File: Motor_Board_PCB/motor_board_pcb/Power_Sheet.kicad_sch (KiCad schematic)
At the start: 16 parts, among them J4 Barrel_Jack, U3 AP2112K-3.3TRG1, U4 AP63205WU-7

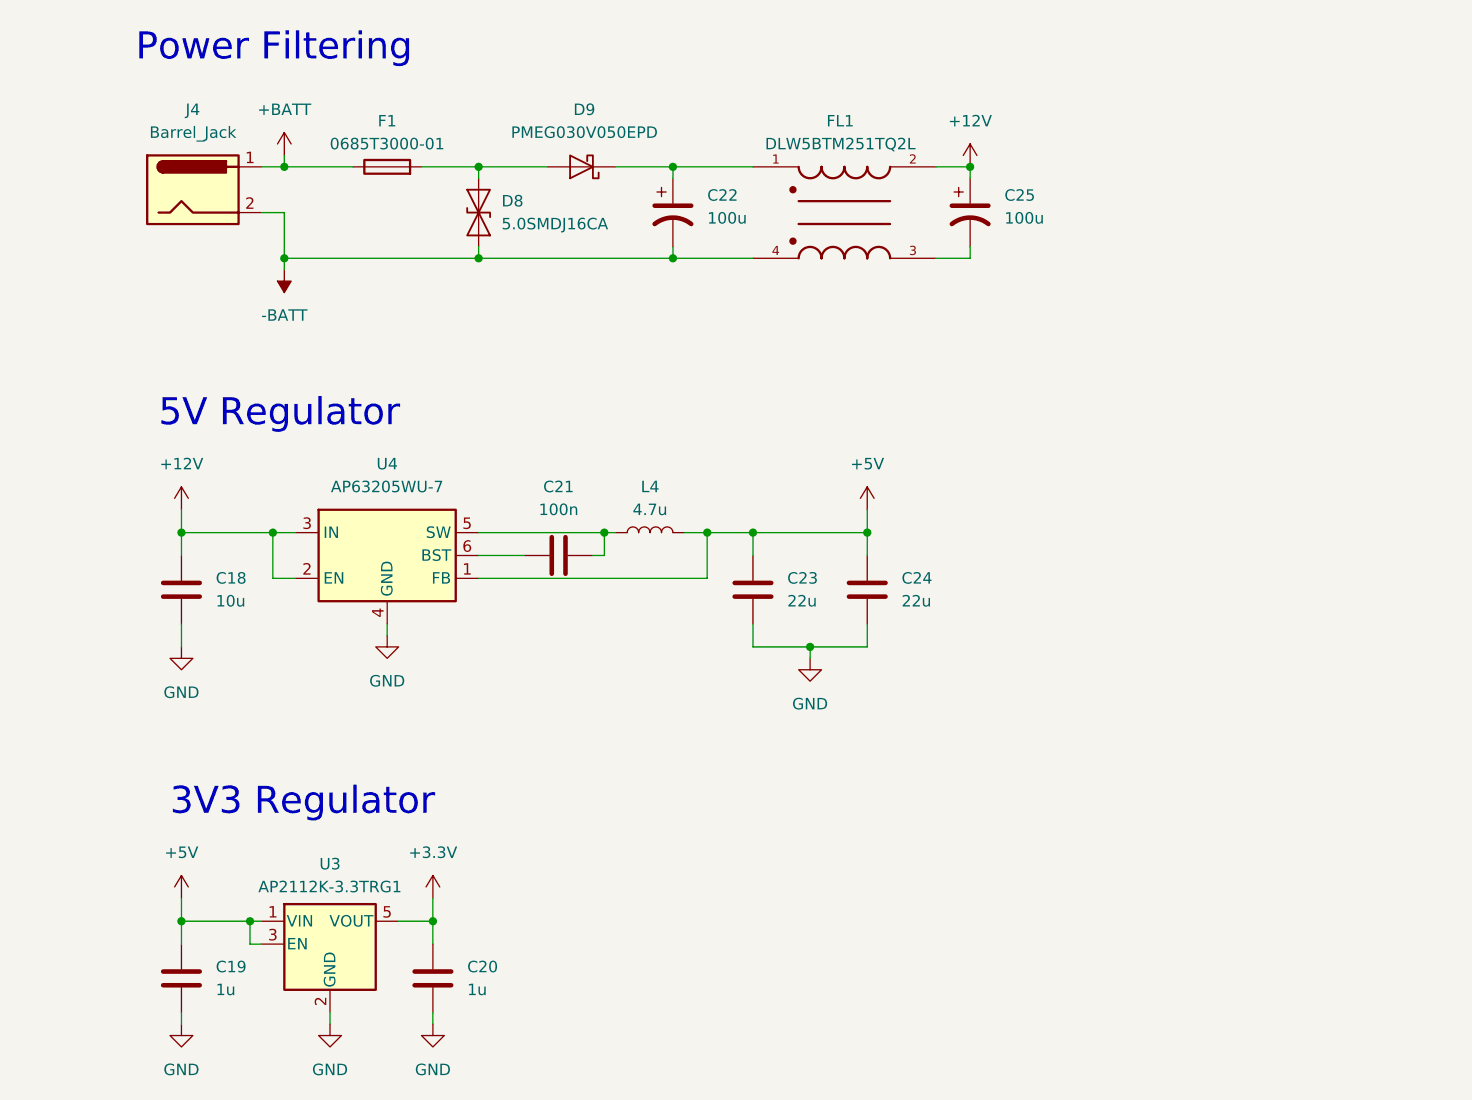
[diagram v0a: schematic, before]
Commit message: Added footprints for almost all components
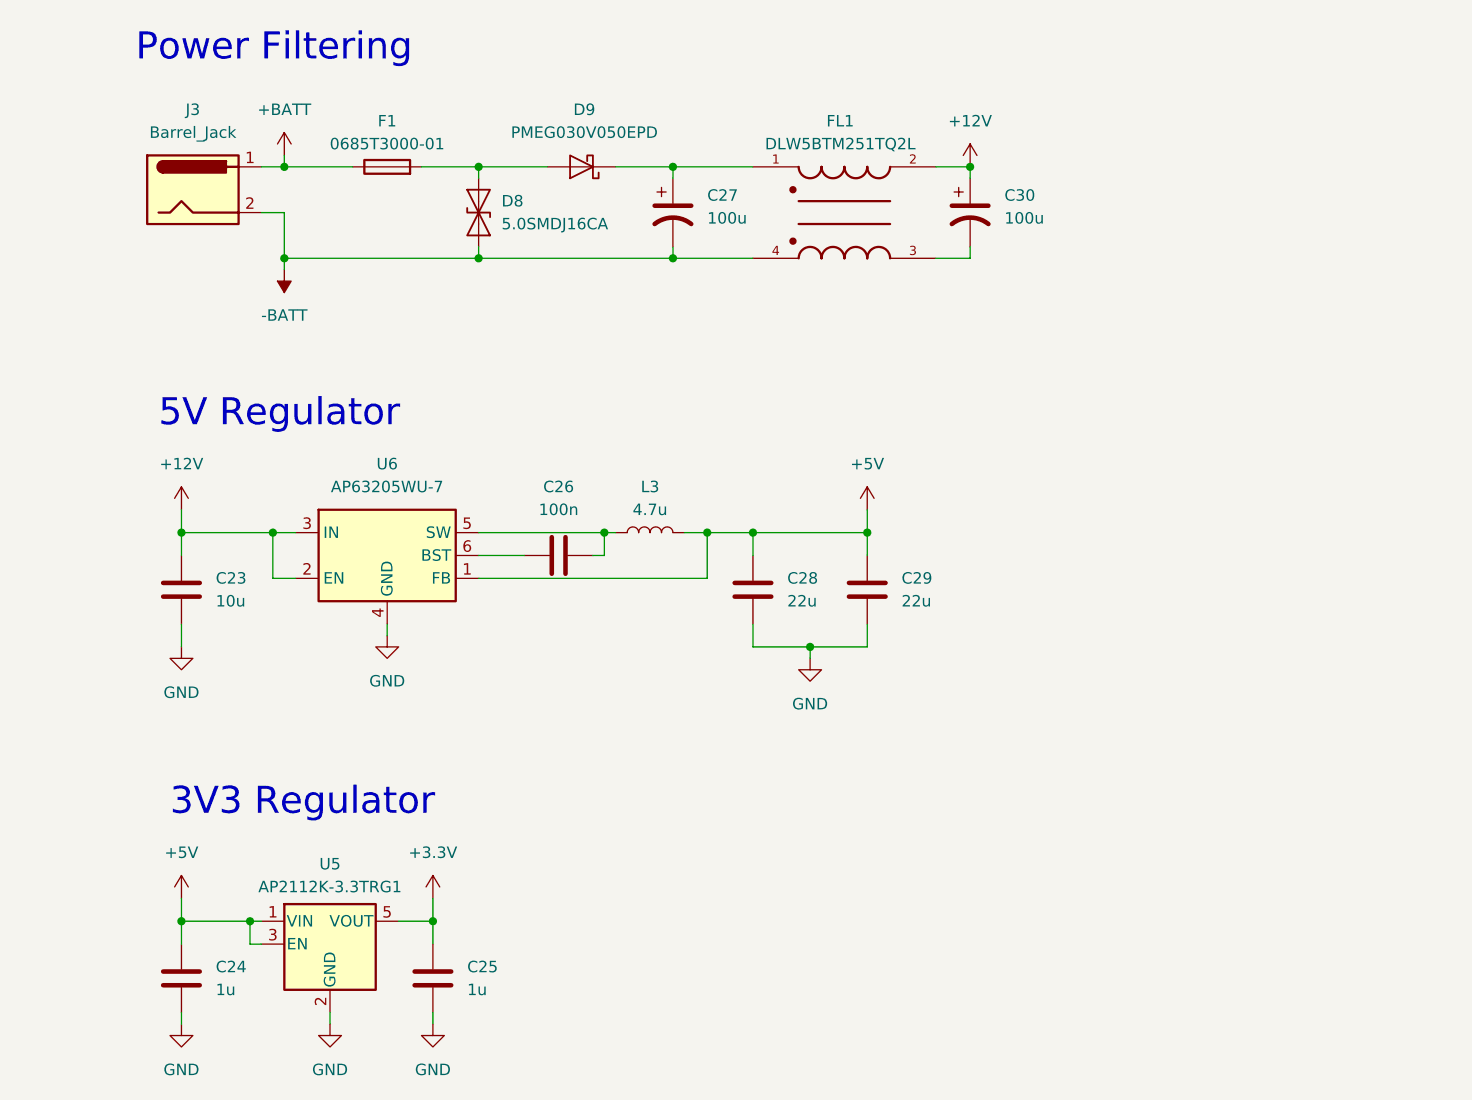
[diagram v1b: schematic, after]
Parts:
- removed J4: Barrel_Jack, symbol Connector:Barrel_Jack
- added J3: Barrel_Jack, Connector_BarrelJack:BarrelJack_CUI_PJ-063AH_Horizontal, symbol Connector:Barrel_Jack
- C23: renamed from C18; footprint (none) -> Capacitor_SMD:C_0603_1608Metric
- C24: renamed from C19; footprint (none) -> Capacitor_SMD:C_0603_1608Metric
- C25: renamed from C20; footprint (none) -> Capacitor_SMD:C_0603_1608Metric
- C26: renamed from C21; footprint (none) -> Capacitor_SMD:C_0603_1608Metric
- C27: renamed from C22; footprint (none) -> Capacitor_SMD:C_0603_1608Metric
- C28: renamed from C23; footprint (none) -> Capacitor_SMD:C_0603_1608Metric
- C29: renamed from C24; footprint (none) -> Capacitor_SMD:C_0603_1608Metric
- C30: renamed from C25; footprint (none) -> Capacitor_SMD:C_0603_1608Metric
- D8: footprint (none) -> Diode_SMD:D_0603_1608Metric
- F1: footprint (none) -> Fuse:Fuse_0603_1608Metric
- FL1: footprint DLW5BTM251TQ2L:FIL_DLW5BTM251TQ2L -> (none)
- renumbered L4 to L3, U3 to U5, U4 to U6
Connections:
- net +BATT: now also J3.1
- net -BATT: now also J3.2

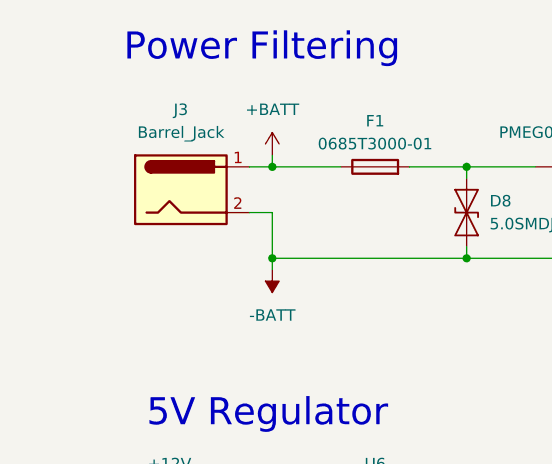
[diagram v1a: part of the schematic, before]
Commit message: Added all other footprints... populated all components with NO errors or warnings :)
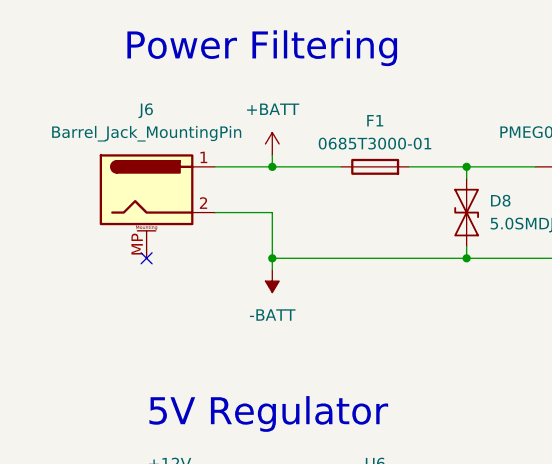
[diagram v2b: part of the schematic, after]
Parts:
- removed J3: Barrel_Jack, Connector_BarrelJack:BarrelJack_CUI_PJ-063AH_Horizontal, symbol Connector:Barrel_Jack
- added J6: Barrel_Jack_MountingPin, Connector_BarrelJack:BarrelJack_CUI_PJ-063AH_Horizontal, symbol Connector:Barrel_Jack_MountingPin
- FL1: footprint (none) -> ~ALL:FIL_DLW5BTZ251TQ2L
- L3: footprint (none) -> ~ALL:INDC2520X120N
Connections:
- net +BATT: now also J6.1
- net -BATT: now also J6.2
- no-connect marks 0 -> 1
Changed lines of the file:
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@@
   (junction (at 68.58 132.08) (diameter 0) (color 0 0 0 0)
   )
+  (no_connect (at 38.1 58.42))
   (wire (pts (xy 104.14 101.6) (xy 110.49 101.6))
     (stroke (width 0) (type default))
@@
     (stroke (width 0) (type default))
   )
-  (wire (pts (xy 49.53 48.26) (xy 52.07 48.26))
+  (wire (pts (xy 45.72 48.26) (xy 52.07 48.26))
     (stroke (width 0) (type default))
   )
@@
     (stroke (width 0) (type default))
   )
-  (wire (pts (xy 49.53 53.34) (xy 52.07 53.34))
-    (stroke (width 0) (type default))
-  )
   (wire (pts (xy 73.66 49.53) (xy 73.66 48.26))
     (stroke (width 0) (type default))
@@
   )
   (wire (pts (xy 52.07 53.34) (xy 52.07 58.42))
+    (stroke (width 0) (type default))
+  )
+  (wire (pts (xy 45.72 53.34) (xy 52.07 53.34))
     (stroke (width 0) (type default))
   )
@@
     )
   )
+  (symbol (lib_id "Connector:Barrel_Jack_MountingPin") (at 38.1 50.8 0) (unit 1)
+    (in_bom yes) (on_board yes) (dnp no) (fields_autoplaced)
+    (property "Reference" "J6" (at 38.1 41.91 0)
+      (effects (font (size 1.27 1.27)))
+    )
+    (property "Value" "Barrel_Jack_MountingPin" (at 38.1 44.45 0)
+      (effects (font (size 1.27 1.27)))
+    )
+    (property "Footprint" "Connector_BarrelJack:BarrelJack_CUI_PJ-063AH_Horizontal" (at 39.37 51.816 0)
+      (effects (font (size 1.27 1.27)) hide)
+    )
+    (property "Datasheet" "~" (at 39.37 51.816 0)
+      (effects (font (size 1.27 1.27)) hide)
+    )
+    (pin "1")
+    (pin "2")
+    (pin "MP")
+    (instances
+      (project "motor_board_pcb"
+        (path "/4ad82a24-c992-45c9-b523-12e12bcd6ced/8b03500d-82ba-403b-affc-552426d5b4ea"
+          (reference "J6") (unit 1)
+        )
+      )
+    )
+  )
   (symbol (lib_id "DLW5BTM251TQ2L:DLW5BTM251TQ2L") (at 114.3 53.34 0) (unit 1)
     (in_bom yes) (on_board yes) (dnp no) (fields_autoplaced)
@@
       (effects (font (size 1.27 1.27)))
     )
-    (property "Footprint" "" (at 114.3 53.34 0)
+    (property "Footprint" "~ALL:FIL_DLW5BTZ251TQ2L" (at 114.3 53.34 0)
       (effects (font (size 1.27 1.27)) (justify bottom) hide)
     )
@@
         (path "/a439ee58-92e3-49e0-a19d-7c5a25d23ba1"
           (reference "#PWR?") (unit 1)
-        )
-      )
-    )
-  )
-  (symbol (lib_id "Connector:Barrel_Jack") (at 41.91 50.8 0) (unit 1)
-    (in_bom yes) (on_board yes) (dnp no) (fields_autoplaced)
-    (property "Reference" "J3" (at 41.91 41.91 0)
-      (effects (font (size 1.27 1.27)))
-    )
-    (property "Value" "Barrel_Jack" (at 41.91 44.45 0)
-      (effects (font (size 1.27 1.27)))
-    )
-    (property "Footprint" "Connector_BarrelJack:BarrelJack_CUI_PJ-063AH_Horizontal" (at 43.18 51.816 0)
-      (effects (font (size 1.27 1.27)) hide)
-    )
-    (property "Datasheet" "~" (at 43.18 51.816 0)
-      (effects (font (size 1.27 1.27)) hide)
-    )
-    (pin "1")
-    (pin "2")
-    (instances
-      (project "motor_board_pcb"
-        (path "/4ad82a24-c992-45c9-b523-12e12bcd6ced/8b03500d-82ba-403b-affc-552426d5b4ea"
-          (reference "J3") (unit 1)
-        )
-      )
-      (project "LocalDesign"
-        (path "/a439ee58-92e3-49e0-a19d-7c5a25d23ba1"
-          (reference "J?") (unit 1)
         )
       )
@@
       (effects (font (size 1.27 1.27)))
     )
-    (property "Footprint" "" (at 92.71 88.9 0)
-      (effects (font (size 1.27 1.27)) hide)
-    )
+    (property "Footprint" "~ALL:INDC2520X120N" (at 92.71 88.9 0)
+      (effects (font (size 1.27 1.27)) hide)
+    )

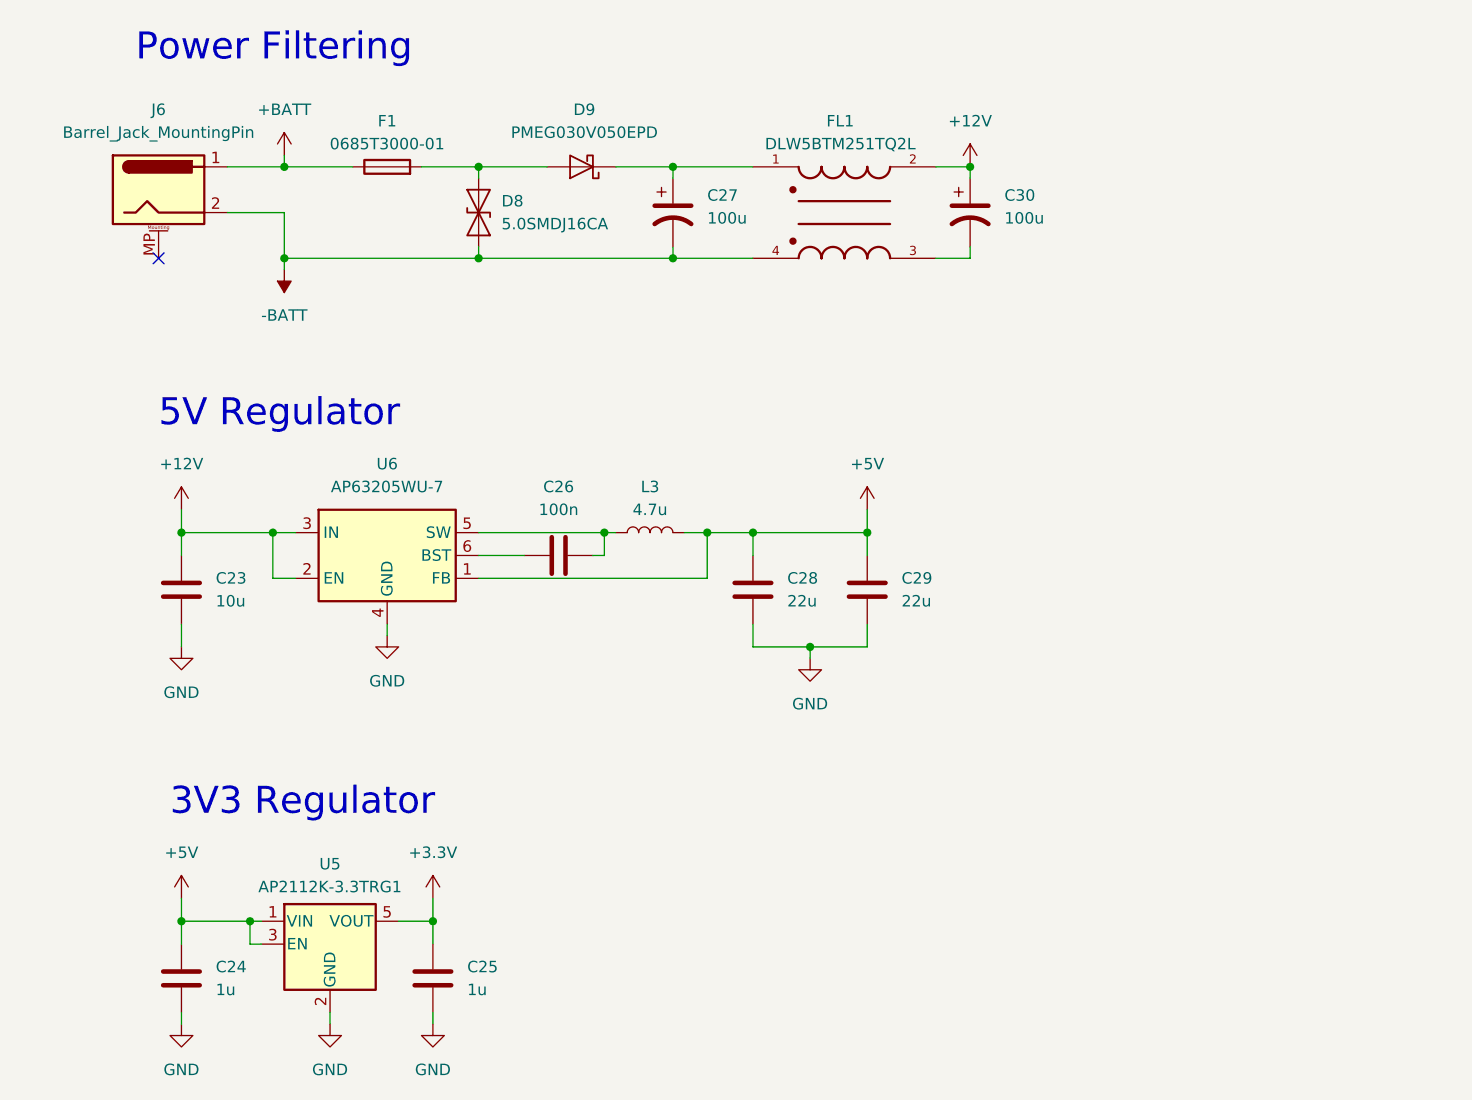
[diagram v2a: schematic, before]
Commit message: Fixed library + power input change
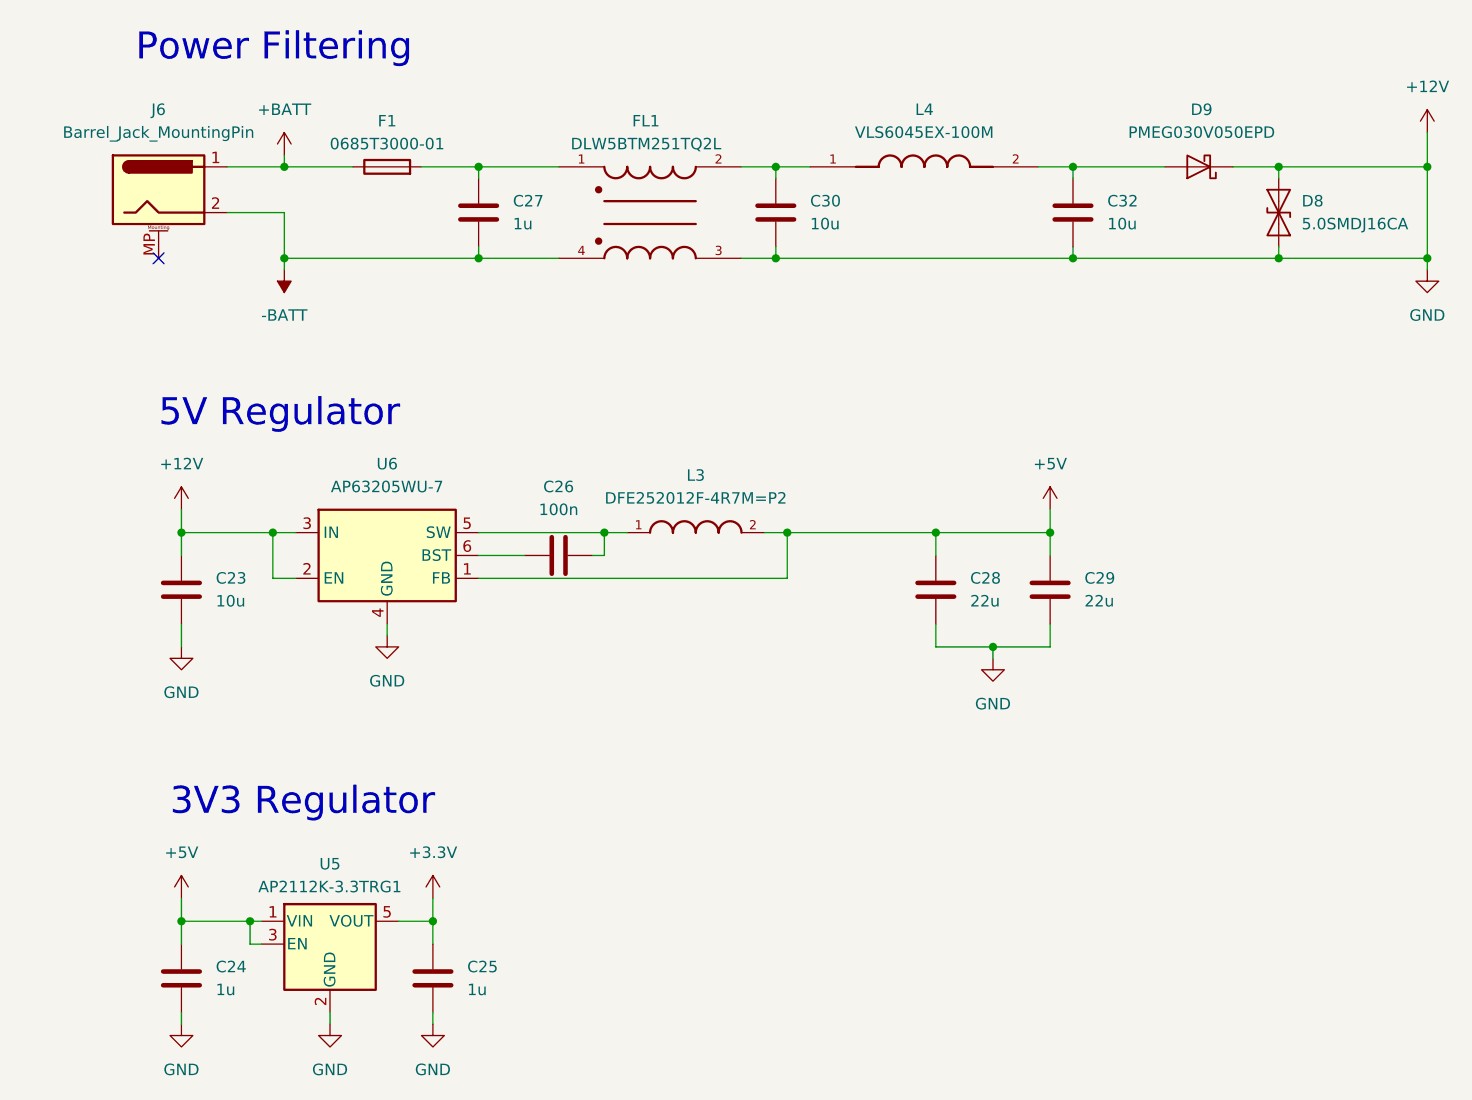
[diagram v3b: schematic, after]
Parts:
- removed C27, C30: 100u, Capacitor_SMD:C_0603_1608Metric, symbol Device:C_Polarized_US
- removed L3: 4.7u, ~ALL:INDC2520X120N, symbol Device:L
- added C27: 1u, Capacitor_SMD:C_1206_3216Metric, symbol Device:C
- added C30, C32: 10u, Capacitor_SMD:C_1210_3225Metric, symbol Device:C
- added L3: DFE252012F-4R7M=P2, ~ALL:INDC2520X120N, symbol DFE252012F-4R7M_P2:DFE252012F-4R7M=P2
- added L4: VLS6045EX-100M, VLS6045EX-100M:IND_VLS6045EX-100M, symbol VLS6045EX-100M:VLS6045EX-100M
- F1: footprint Fuse:Fuse_0603_1608Metric -> Fuse:Fuse_1206_3216Metric
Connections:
- net GND is gone; now on net +12V: C23.1, C24.1, C25.1, C28.1, C29.1, U5.2 (GND), U6.4 (GND)
- net +12V: now also D8.1 (A1), D8.2 (A2), D9.3 (K), FL1.3, C30.1, C32.1; no longer FL1.2
- net +5V: now also L3.2
- net -BATT: now also C27.1; no longer D8.1 (A1)
- net at D9.1 (A), D9.2 (A): now also C32.2, L4.2; no longer D8.2 (A2), F1.2
- net at C26.2, U6.5 (SW): now also L3.1
- net at FL1.1: now also F1.2, C27.2; no longer D9.3 (K)
- new net: C30.2, FL1.2, L4.1
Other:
- moved on the sheet: C28, C29, FL1

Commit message: Library issue fix
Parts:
- L4: footprint VLS6045EX-100M:IND_VLS6045EX-100M -> ~ALL:IND_VLS6045EX-100M
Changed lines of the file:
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@@
       (effects (font (size 1.27 1.27)))
     )
-    (property "Footprint" "VLS6045EX-100M:IND_VLS6045EX-100M" (at 123.19 48.26 0)
+    (property "Footprint" "~ALL:IND_VLS6045EX-100M" (at 123.19 48.26 0)
       (effects (font (size 1.27 1.27)) (justify bottom) hide)
     )

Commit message: Initial PCB placement for Motor Board
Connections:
- net +12V: no longer C23.1, C24.1, C25.1, C28.1, C29.1, C30.1, C32.1, D8.1 (A1), FL1.3, U5.2 (GND), U6.4 (GND)
- new net GND: C23.1, C24.1, C25.1, C28.1, C29.1, C30.1, C32.1, D8.1 (A1), FL1.3, U5.2 (GND), U6.4 (GND)
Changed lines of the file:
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@@
   (junction (at 139.7 58.42) (diameter 0) (color 0 0 0 0)
-  )
-  (junction (at 179.07 48.26) (diameter 0) (color 0 0 0 0)
   )
   (junction (at 130.81 101.6) (diameter 0) (color 0 0 0 0)
@@
   )
   (junction (at 107.95 88.9) (diameter 0) (color 0 0 0 0)
-  )
-  (junction (at 179.07 58.42) (diameter 0) (color 0 0 0 0)
   )
   (junction (at 73.66 58.42) (diameter 0) (color 0 0 0 0)
@@
     (stroke (width 0) (type default))
   )
-  (wire (pts (xy 179.07 48.26) (xy 179.07 58.42))
-    (stroke (width 0) (type default))
-  )
